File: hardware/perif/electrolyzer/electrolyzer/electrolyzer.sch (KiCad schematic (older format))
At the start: 0 parts

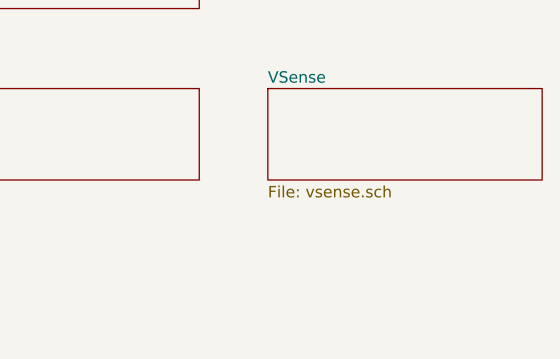
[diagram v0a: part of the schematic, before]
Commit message: Started Electrolyzer board
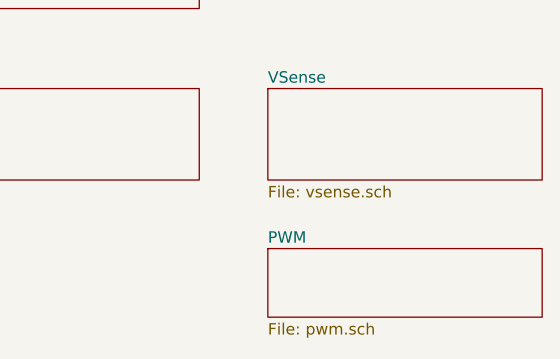
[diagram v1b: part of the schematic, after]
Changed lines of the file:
@@
 $Descr A4 11693 8268
 encoding utf-8
-Sheet 1 3
+Sheet 1 5
 Title ""
 Date ""
@@
 F1 "vsense.sch" 50
 $EndSheet
+$Sheet
+S 3850 3450 1200 300
+U 5F2031FC
+F0 "PWM" 50
+F1 "pwm.sch" 50
+$EndSheet
 $EndSCHEMATC

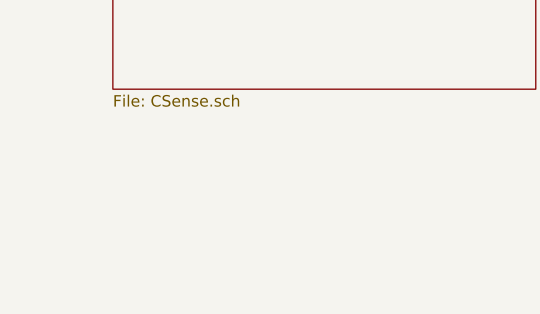
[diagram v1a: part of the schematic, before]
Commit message: Started Electrolyzer board: sense
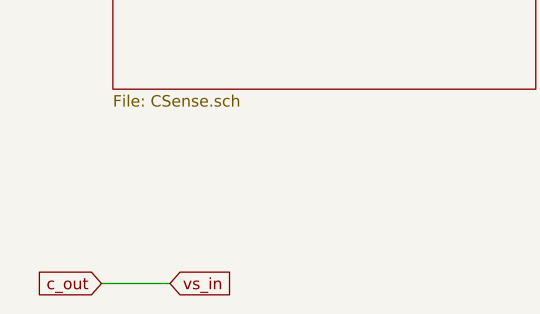
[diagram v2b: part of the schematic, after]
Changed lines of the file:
@@
 F1 "pwm.sch" 50
 $EndSheet
+Text GLabel 1650 4000 0    50   Input ~ 0
+c_out
+Text GLabel 1950 4000 2    50   Input ~ 0
+vs_in
+Wire Wire Line
+	1650 4000 1950 4000
 $EndSCHEMATC
